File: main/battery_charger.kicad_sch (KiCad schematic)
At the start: 48 parts, among them Q1601 IXTP28P065T, Q1602 TK4R3E06PL, Q1603 IRLML0030, Q1604 IXTP28P065T, Q1605 IXTP28P065T, Q1606 IRLML0030, U1601 LT8710, U1602 TMCS1101, U1603 TSV911xxLx

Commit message: Route of power rails
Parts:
- removed Q1604, Q1605: IXTP28P065T, Package_TO_SOT_THT:TO-220-3_Horizontal_TabUp, symbol Device:Q_PMOS_GDS
- added C1616: 10u, Capacitor_SMD:C_0805_2012Metric, symbol Device:C
- added C1617: 100n, Capacitor_SMD:C_0805_2012Metric, symbol Device:C
- added Q1604, Q1605: FDS6681Z, Package_SO:SOIC-8_3.9x4.9mm_P1.27mm, symbol dsv4:FDS6681Z
- added R1615: 10k, Resistor_SMD:R_0805_2012Metric, symbol Device:R
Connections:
- net +3.3V: now also R1615.1
- net PGND: now also C1616.2, C1617.2
- net RETURN_PATH_OUT: now also Q1604.1 (S), Q1604.2 (S), Q1604.3 (S)
- net V_{IN}: now also C1616.1, C1617.1
- net BATT_OK: now reaches U1601.4 (FLAG)
- net BATT_OK: now also R1615.2
- net SWOUT_ISP: now reaches Q1601.3 (S), R1601.1, U1601.7 (ISP)
- net at D1603.2 (A), R1611.2: now also Q1604.4 (G)
- net at D1604.2 (A), R1612.2: now also Q1605.4 (G)
- net BATT_RET_PATH: now reaches R1612.1, U1602.3 (OUT), U1602.4 (OUT)
- net BATT_RET_PATH: now also Q1605.1 (S), Q1605.2 (S), Q1605.3 (S)
- new net BAT_RET_MID: Q1604.5 (D), Q1604.6 (D), Q1604.7 (D), Q1604.8 (D), Q1605.5 (D), Q1605.6 (D), Q1605.7 (D), Q1605.8 (D)
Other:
- moved on the sheet: Q1602, R1602

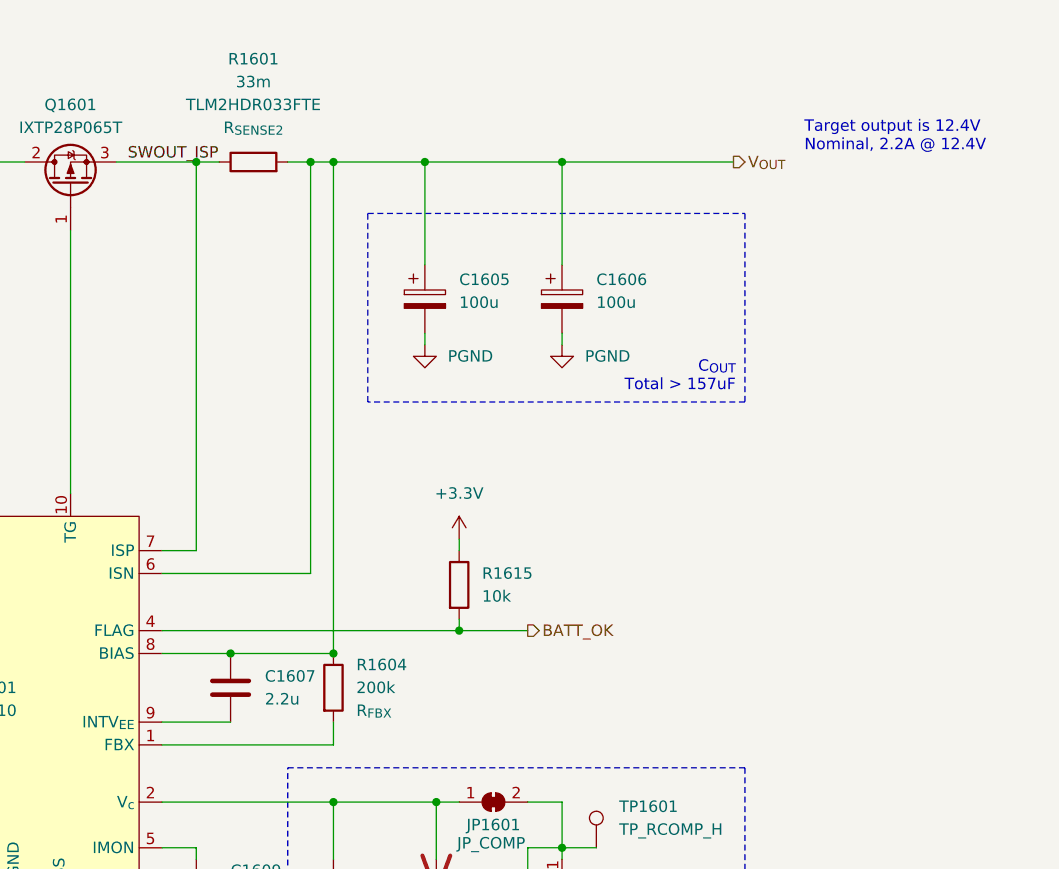
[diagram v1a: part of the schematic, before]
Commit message: Power routed
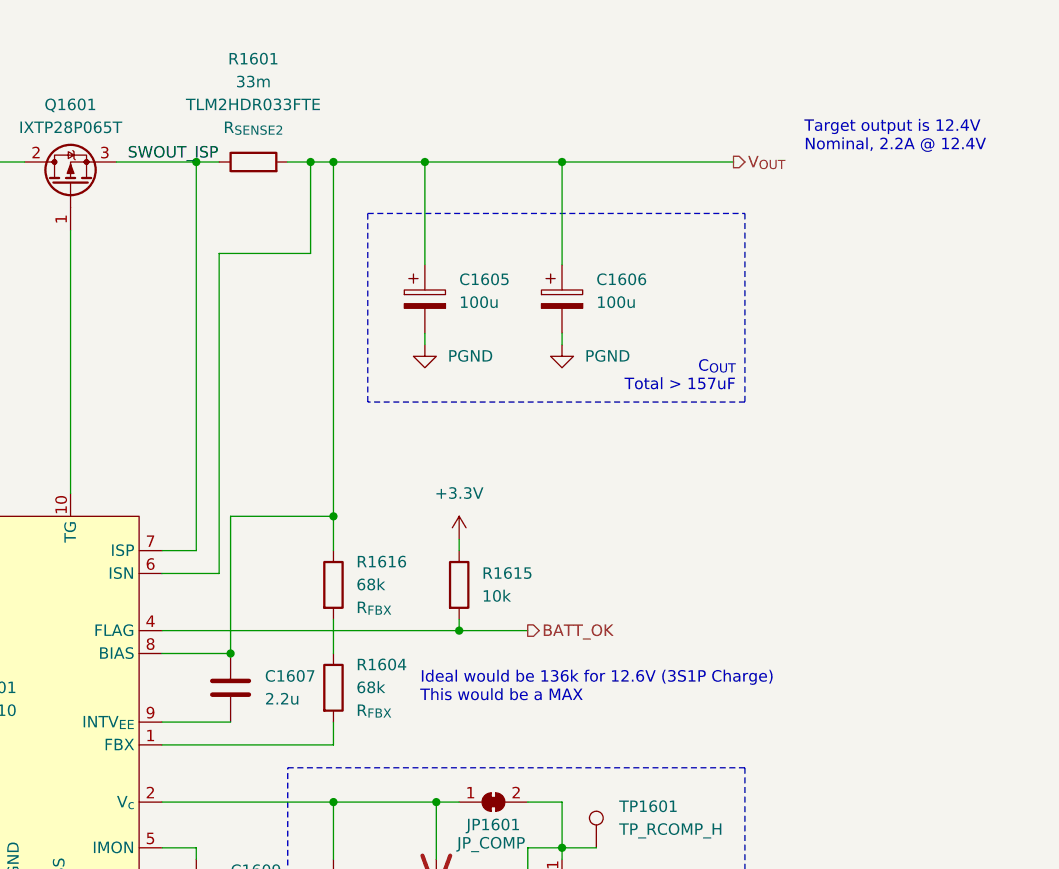
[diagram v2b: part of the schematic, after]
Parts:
- added R1616: 68k, Resistor_SMD:R_0805_2012Metric, symbol Device:R
- R1604: value 200k -> 68k
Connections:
- net V_{OUT}: now also R1616.1; no longer R1604.1
- new net: R1604.1, R1616.2
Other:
- note added: "Ideal would be 136k for 12.6V (3S1P Charge) This would be a MAX"

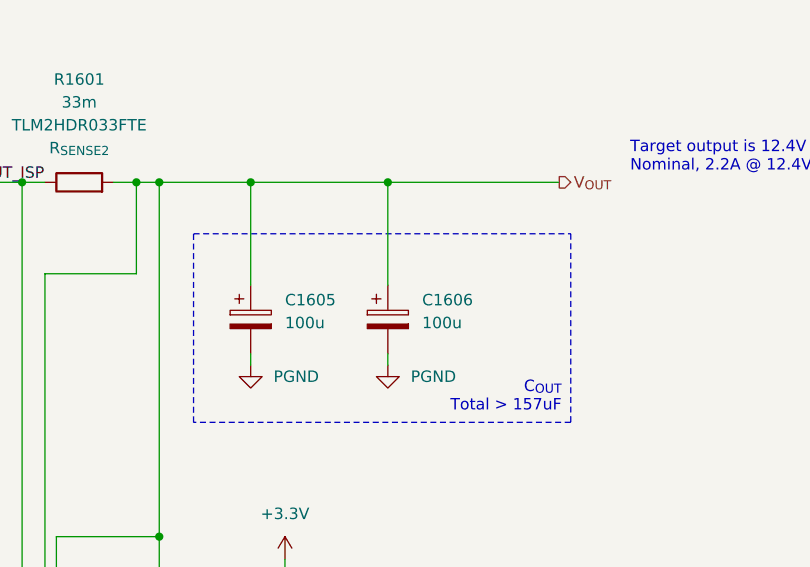
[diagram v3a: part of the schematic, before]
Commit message: Rework north route
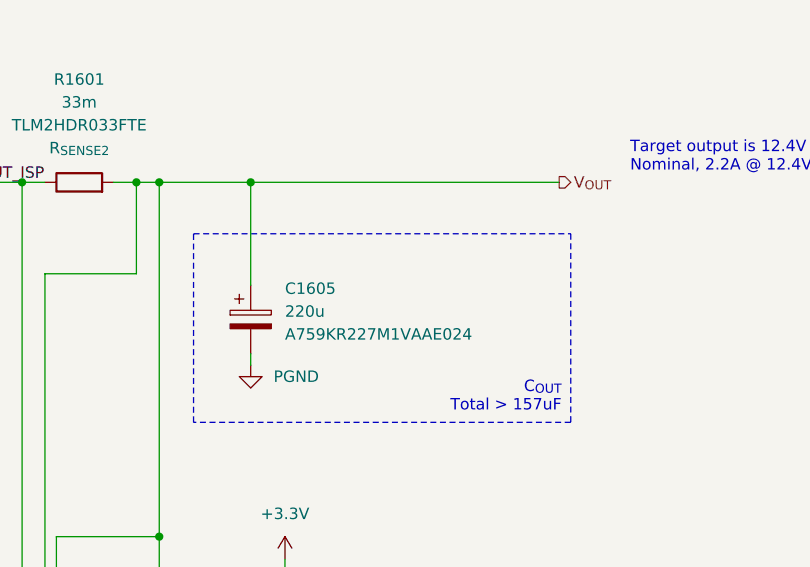
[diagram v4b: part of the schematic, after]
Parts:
- removed C1606: 100u, Capacitor_THT:CP_Radial_D6.3mm_P2.50mm, symbol Device:C_Polarized
- C1605: value 100u -> 220u; footprint Capacitor_THT:CP_Radial_D6.3mm_P2.50mm -> Capacitor_THT:CP_Radial_D8.0mm_P3.50mm; MPN (none) -> A759KR227M1VAAE024
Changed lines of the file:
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@@
 	)
 	(junction
-		(at 213.36 34.29)
-		(diameter 0)
-		(color 0 0 0 0)
-	)
-	(junction
 		(at 199.39 105.41)
 		(diameter 0)
@@
 	(wire
 		(pts
-			(xy 198.12 34.29) (xy 213.36 34.29)
+			(xy 198.12 34.29) (xy 232.41 34.29)
 		)
 		(stroke
@@
 	(wire
 		(pts
-			(xy 213.36 54.61) (xy 213.36 53.34)
-		)
-		(stroke
-			(width 0)
-			(type default)
-		)
-	)
-	(wire
-		(pts
 			(xy 73.66 168.91) (xy 66.04 168.91)
 		)
@@
 	(wire
 		(pts
-			(xy 213.36 34.29) (xy 232.41 34.29)
-		)
-		(stroke
-			(width 0)
-			(type default)
-		)
-	)
-	(wire
-		(pts
 			(xy 73.66 54.61) (xy 73.66 52.07)
 		)
@@
 	(wire
 		(pts
-			(xy 213.36 34.29) (xy 213.36 45.72)
-		)
-		(stroke
-			(width 0)
-			(type default)
-		)
-	)
-	(wire
-		(pts
 			(xy 187.96 77.47) (xy 187.96 73.66)
 		)
@@
 	)
 	(symbol
-		(lib_id "Device:C_Polarized")
-		(at 213.36 49.53 0)
-		(unit 1)
-		(exclude_from_sim no)
-		(in_bom yes)
-		(on_board yes)
-		(dnp no)
-		(fields_autoplaced yes)
-		(property "Reference" "C1606"
-			(at 217.17 47.3709 0)
-			(effects
-				(font
-					(size 1.27 1.27)
-				)
-				(justify left)
-			)
-		)
-		(property "Value" "100u"
-			(at 217.17 49.9109 0)
-			(effects
-				(font
-					(size 1.27 1.27)
-				)
-				(justify left)
-			)
-		)
-		(property "Footprint" "Capacitor_THT:CP_Radial_D6.3mm_P2.50mm"
-			(at 214.3252 53.34 0)
-			(effects
-				(font
-					(size 1.27 1.27)
-				)
-				(hide yes)
-			)
-		)
-		(property "Datasheet" "~"
-			(at 213.36 49.53 0)
-			(effects
-				(font
-					(size 1.27 1.27)
-				)
-				(hide yes)
-			)
-		)
-		(property "Description" "Polarized capacitor"
-			(at 213.36 49.53 0)
-			(effects
-				(font
-					(size 1.27 1.27)
-				)
-				(hide yes)
-			)
-		)
-		(pin "1"
-		)
-		(pin "2"
-		)
-		(instances
-			(project "dsv4"
-				(path "/c07e9297-fde8-4755-803e-d05072cd6096/164e5be8-13e0-4d66-ab9d-977f2147e774/2568eb76-a76e-4dca-9ea6-ce4815cb5838"
-					(reference "C1606")
-					(unit 1)
-				)
-			)
-		)
-	)
-	(symbol
 		(lib_id "power:GNDD")
 		(at 148.59 180.34 0)
@@
 	)
 	(symbol
-		(lib_id "power:GND")
-		(at 213.36 54.61 0)
-		(unit 1)
-		(exclude_from_sim no)
-		(in_bom yes)
-		(on_board yes)
-		(dnp no)
-		(fields_autoplaced yes)
-		(property "Reference" "#PWR01605"
-			(at 213.36 59.69 0)
-			(effects
-				(font
-					(size 1.27 1.27)
-				)
-				(hide yes)
-			)
-		)
-		(property "Value" "PGND"
-			(at 215.9 55.8799 0)
-			(effects
-				(font
-					(size 1.27 1.27)
-				)
-				(justify left)
-			)
-		)
-		(property "Footprint" ""
-			(at 213.36 54.61 0)
-			(effects
-				(font
-					(size 1.27 1.27)
-				)
-				(hide yes)
-			)
-		)
-		(property "Datasheet" ""
-			(at 213.36 54.61 0)
-			(effects
-				(font
-					(size 1.27 1.27)
-				)
-				(hide yes)
-			)
-		)
-		(property "Description" "Power symbol creates a global label with name \"GND\" , ground"
-			(at 213.36 54.61 0)
-			(effects
-				(font
-					(size 1.27 1.27)
-				)
-				(hide yes)
-			)
-		)
-		(pin "1"
-		)
-		(instances
-			(project "dsv4"
-				(path "/c07e9297-fde8-4755-803e-d05072cd6096/164e5be8-13e0-4d66-ab9d-977f2147e774/2568eb76-a76e-4dca-9ea6-ce4815cb5838"
-					(reference "#PWR01605")
-					(unit 1)
-				)
-			)
-		)
-	)
-	(symbol
 		(lib_id "Device:C")
 		(at 111.76 68.58 0)
@@
 		(fields_autoplaced yes)
 		(property "Reference" "C1605"
-			(at 201.93 47.3709 0)
+			(at 201.93 46.1009 0)
 			(effects
 				(font
@@
 			)
 		)
-		(property "Value" "100u"
-			(at 201.93 49.9109 0)
+		(property "Value" "220u"
+			(at 201.93 48.6409 0)
 			(effects
 				(font
@@
 			)
 		)
-		(property "Footprint" "Capacitor_THT:CP_Radial_D6.3mm_P2.50mm"
+		(property "Footprint" "Capacitor_THT:CP_Radial_D8.0mm_P3.50mm"
 			(at 199.0852 53.34 0)
 			(effects
@@
 			)
 		)
-		(property "Datasheet" "~"
+		(property "Datasheet" "https://www.mouser.fr/datasheet/2/447/KEM_A4072_A759-3316694.pdf"
 			(at 198.12 49.53 0)
 			(effects
@@
 			)
 		)
+		(property "MPN" "A759KR227M1VAAE024"
+			(at 201.93 51.1809 0)
+			(effects
+				(font
+					(size 1.27 1.27)
+				)
+				(justify left)
+			)
+		)
+		(property "Name" ""
+			(at 198.12 49.53 0)
+			(effects
+				(font
+					(size 1.27 1.27)
+				)
+			)
+		)

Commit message: More routing
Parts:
- added C1606: 100n, Capacitor_SMD:C_0805_2012Metric, symbol Device:C
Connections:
- net +3.3V: now also C1606.1
- net GNDD: now also C1606.2
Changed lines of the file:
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@@
 	)
 	(symbol
+		(lib_id "power:+3.3V")
+		(at 163.83 180.34 0)
+		(unit 1)
+		(exclude_from_sim no)
+		(in_bom yes)
+		(on_board yes)
+		(dnp no)
+		(fields_autoplaced yes)
+		(property "Reference" "#PWR01625"
+			(at 163.83 184.15 0)
+			(effects
+				(font
+					(size 1.27 1.27)
+				)
+				(hide yes)
+			)
+		)
+		(property "Value" "+3.3V"
+			(at 163.83 175.26 0)
+			(effects
+				(font
+					(size 1.27 1.27)
+				)
+			)
+		)
+		(property "Footprint" ""
+			(at 163.83 180.34 0)
+			(effects
+				(font
+					(size 1.27 1.27)
+				)
+				(hide yes)
+			)
+		)
+		(property "Datasheet" ""
+			(at 163.83 180.34 0)
+			(effects
+				(font
+					(size 1.27 1.27)
+				)
+				(hide yes)
+			)
+		)
+		(property "Description" "Power symbol creates a global label with name \"+3.3V\""
+			(at 163.83 180.34 0)
+			(effects
+				(font
+					(size 1.27 1.27)
+				)
+				(hide yes)
+			)
+		)
+		(pin "1"
+		)
+		(instances
+			(project "dsv4"
+				(path "/c07e9297-fde8-4755-803e-d05072cd6096/164e5be8-13e0-4d66-ab9d-977f2147e774/2568eb76-a76e-4dca-9ea6-ce4815cb5838"
+					(reference "#PWR01625")
+					(unit 1)
+				)
+			)
+		)
+	)
+	(symbol
 		(lib_id "Device:R")
 		(at 115.57 162.56 0)
@@
 	(symbol
 		(lib_id "Device:C")
+		(at 163.83 184.15 0)
+		(unit 1)
+		(exclude_from_sim no)
+		(in_bom yes)
+		(on_board yes)
+		(dnp no)
+		(fields_autoplaced yes)
+		(property "Reference" "C1606"
+			(at 167.64 182.8799 0)
+			(effects
+				(font
+					(size 1.27 1.27)
+				)
+				(justify left)
+			)
+		)
+		(property "Value" "100n"
+			(at 167.64 185.4199 0)
+			(effects
+				(font
+					(size 1.27 1.27)
+				)
+				(justify left)
+			)
+		)
+		(property "Footprint" "Capacitor_SMD:C_0805_2012Metric"
+			(at 164.7952 187.96 0)
+			(effects
+				(font
+					(size 1.27 1.27)
+				)
+				(hide yes)
+			)
+		)
+		(property "Datasheet" "~"
+			(at 163.83 184.15 0)
+			(effects
+				(font
+					(size 1.27 1.27)
+				)
+				(hide yes)
+			)
+		)
+		(property "Description" "Unpolarized capacitor"
+			(at 163.83 184.15 0)
+			(effects
+				(font
+					(size 1.27 1.27)
+				)
+				(hide yes)
+			)
+		)
+		(pin "2"
+		)
+		(pin "1"
+		)
+		(instances
+			(project "dsv4"
+				(path "/c07e9297-fde8-4755-803e-d05072cd6096/164e5be8-13e0-4d66-ab9d-977f2147e774/2568eb76-a76e-4dca-9ea6-ce4815cb5838"
+					(reference "C1606")
+					(unit 1)
+				)
+			)
+		)
+	)
+	(symbol
+		(lib_id "Device:C")
 		(at 111.76 68.58 0)
 		(unit 1)
@@
 					(unit 1)
 				)
+			)
+		)
+	)
+	(symbol
+		(lib_id "power:GNDD")
+		(at 163.83 187.96 0)
+		(unit 1)
+		(exclude_from_sim no)
+		(in_bom yes)
+		(on_board yes)
+		(dnp no)
+		(fields_autoplaced yes)
+		(property "Reference" "#PWR01605"
+			(at 163.83 194.31 0)
+			(effects
+				(font
+					(size 1.27 1.27)
+				)
+				(hide yes)
+			)
+		)
+		(property "Value" "GNDD"
+			(at 163.83 191.77 0)
+			(effects
+				(font
+					(size 1.27 1.27)
+				)
+			)
+		)
+		(property "Footprint" ""
+			(at 163.83 187.96 0)
+			(effects
+				(font
+					(size 1.27 1.27)
+				)
+				(hide yes)
+			)
+		)
+		(property "Datasheet" ""
+			(at 163.83 187.96 0)
+			(effects
+				(font
+					(size 1.27 1.27)
+				)
+				(hide yes)
+			)
+		)
+		(property "Description" "Power symbol creates a global label with name \"GNDD\" , digital ground"
+			(at 163.83 187.96 0)
+			(effects
+				(font
+					(size 1.27 1.27)
+				)
+				(hide yes)
+			)
+		)
+		(pin "1"
+		)
+		(instances
+			(project "dsv4"
+				(path "/c07e9297-fde8-4755-803e-d05072cd6096/164e5be8-13e0-4d66-ab9d-977f2147e774/2568eb76-a76e-4dca-9ea6-ce4815cb5838"
+					(reference "#PWR01605")
+					(unit 1)
+				)
